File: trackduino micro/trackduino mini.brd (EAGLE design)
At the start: 48.1 x 21.9 mm, 28 parts, among them IC2 74AHC1G125DBV, SW1 SPST_TACT-KMR2, U1 ATMEGA168, Y1 16MHZ

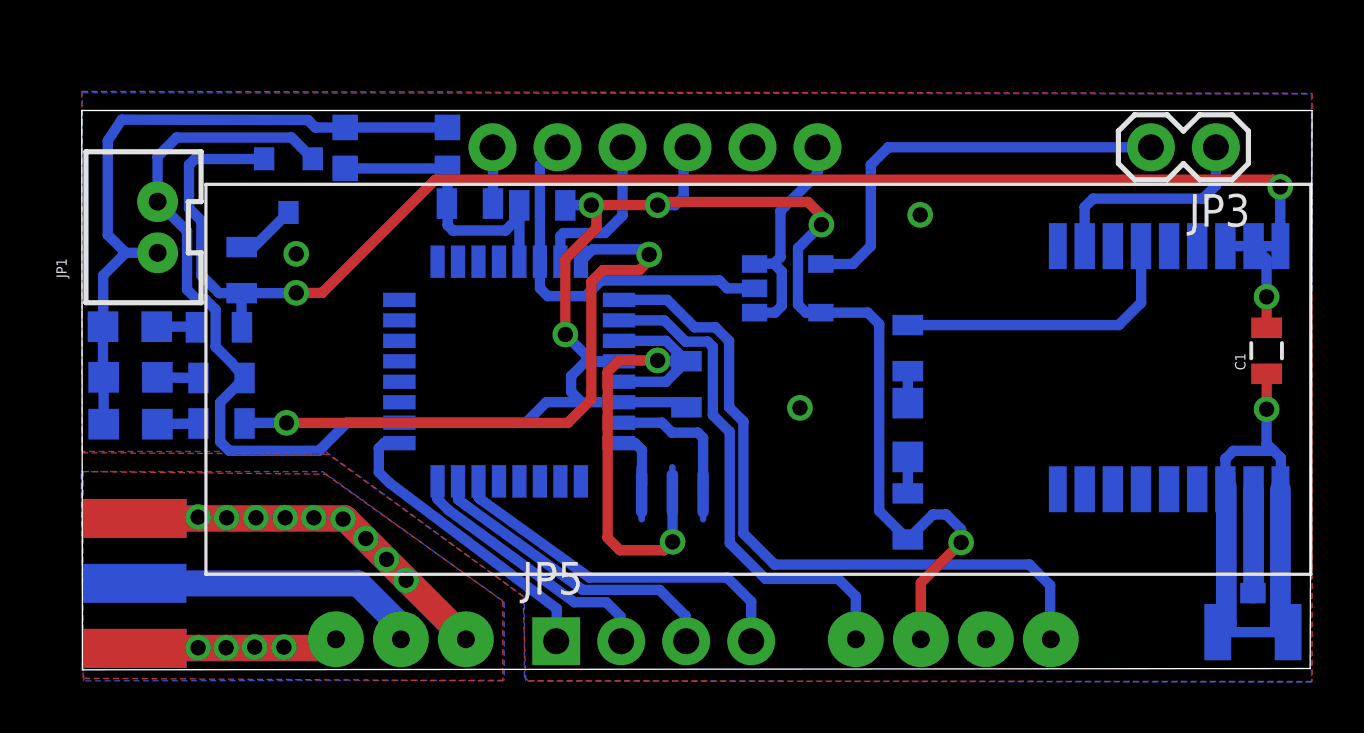
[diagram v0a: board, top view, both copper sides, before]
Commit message: Revert 8864008..107cc9b
This rolls back to commit 8864008ccbdc4df3da8dbd79e6a63e8a5caf342f.
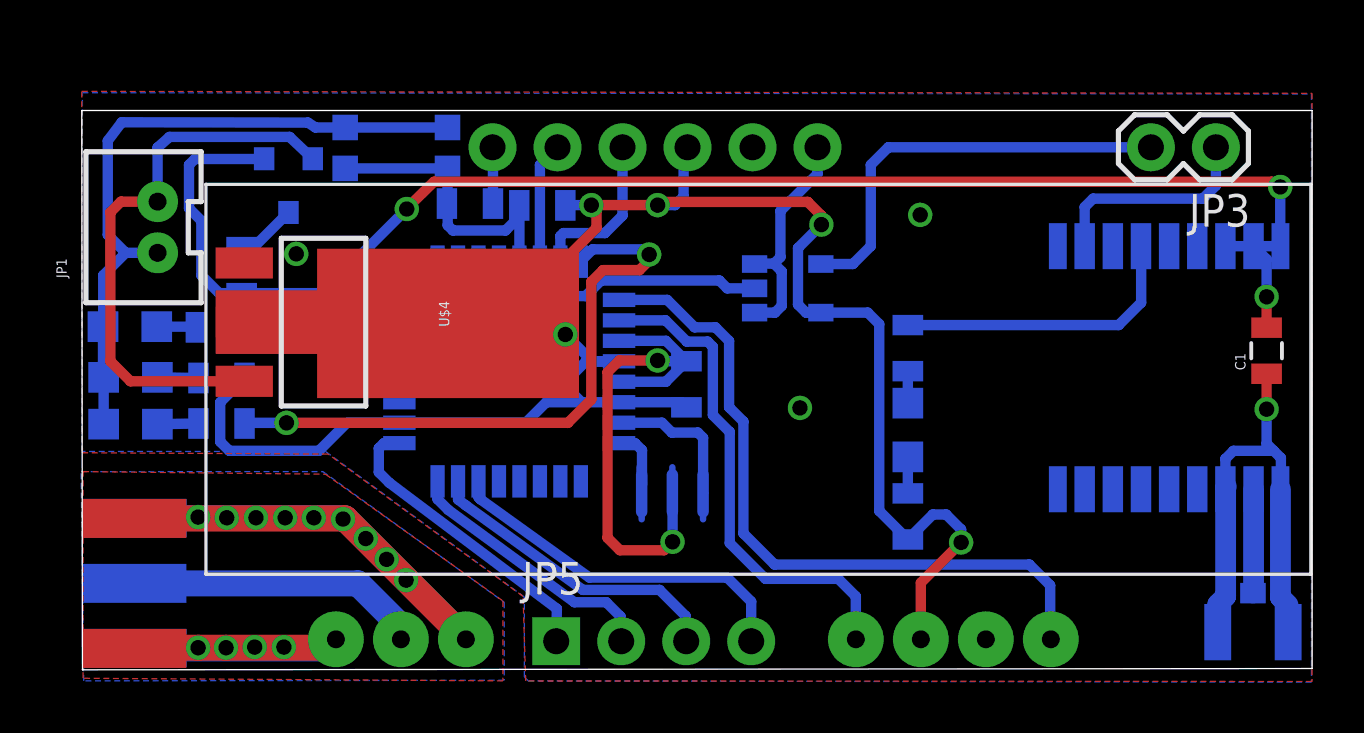
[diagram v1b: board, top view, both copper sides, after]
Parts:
- added U$4: V_REG_MIC2920, SparkFun-PowerIC:SOT223
- C5: value (none) -> 100n
- R1, R3: value (none) -> 100
- R4, R6: value (none) -> 330
- R5: value (none) -> 10k
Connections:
- new net 15V: JP1.2, U$3.2, U$4.3
- net GND: now also U$4.1
- net VCC: now also U$4.2; no longer JP1.2, U$3.2
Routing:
- net 15V: track 0.00 -> 22.1 mm
- net VCC: track 87.9 -> 83.7 mm
- net GND: track 127.9 -> 123.9 mm, vias 5 -> 8
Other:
- outline, holes or cut-outs redrawn

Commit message: trackuino rev1
Fixed errors found after assembling the first prototype
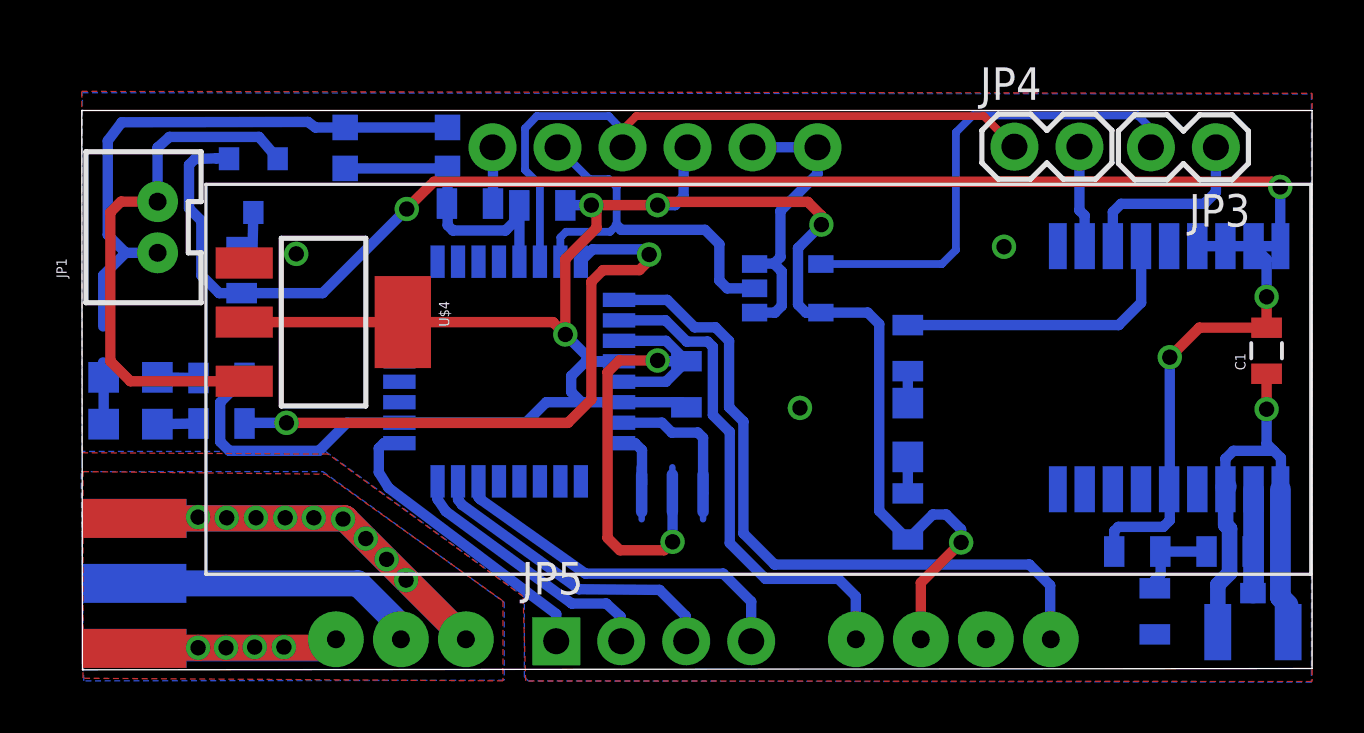
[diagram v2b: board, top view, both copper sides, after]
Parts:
- removed LED2: (no value), adafruit:CHIP-LED0805
- removed R3: 100, SparkFun-Resistors:0805
- added C6: (no value), SparkFun-Capacitors:0805
- added JP4: M02PTH, SparkFun-Connectors:1X02
- added L1: (no value), SparkFun-Passives:0805
- added R2: 100, SparkFun-Resistors:0805
- moved U$3 1.37 mm to (53.3, 76.4)
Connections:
- net TX-3V3 renamed TX1
- removed net CTS: JP2.5
- removed net N$7: LED2.A, R3.1
- new net N$24: C6.1, L1.2, R2.1
- net 3V: now also R2.2, U$1.14_VCC_RF, U$1.6_V_BCKP; no longer R3.2
- net GND: now also C6.2, JP2.5; no longer LED2.C
- net N$6: now also L1.1
- net RX: now also JP3.1
- net RXO: now also JP2.3, JP4.1; no longer IC2.2, JP2.2
- net TX: now also JP4.2; no longer JP3.1
- net TXO: now also IC2.2, JP2.2; no longer JP2.3
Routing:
- net RXO: track 14.7 -> 27.1 mm
- net 3V: track 61.1 -> 73.3 mm, vias 3 -> 4
- net TXO: track 6.43 -> 15.0 mm
- net RX: track 0.00 -> 7.44 mm
- net TX: track 8.50 -> 3.97 mm
- net N$24: track 0.00 -> 3.34 mm
- net TX1: track 16.6 -> 18.9 mm
- net N$6: track 4.07 -> 5.70 mm
- net N$7: track 1.54 -> 0.00 mm
- net 15V: track 22.1 -> 20.8 mm
- net GND: track 123.9 -> 124.6 mm
